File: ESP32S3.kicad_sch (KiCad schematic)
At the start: 0 parts

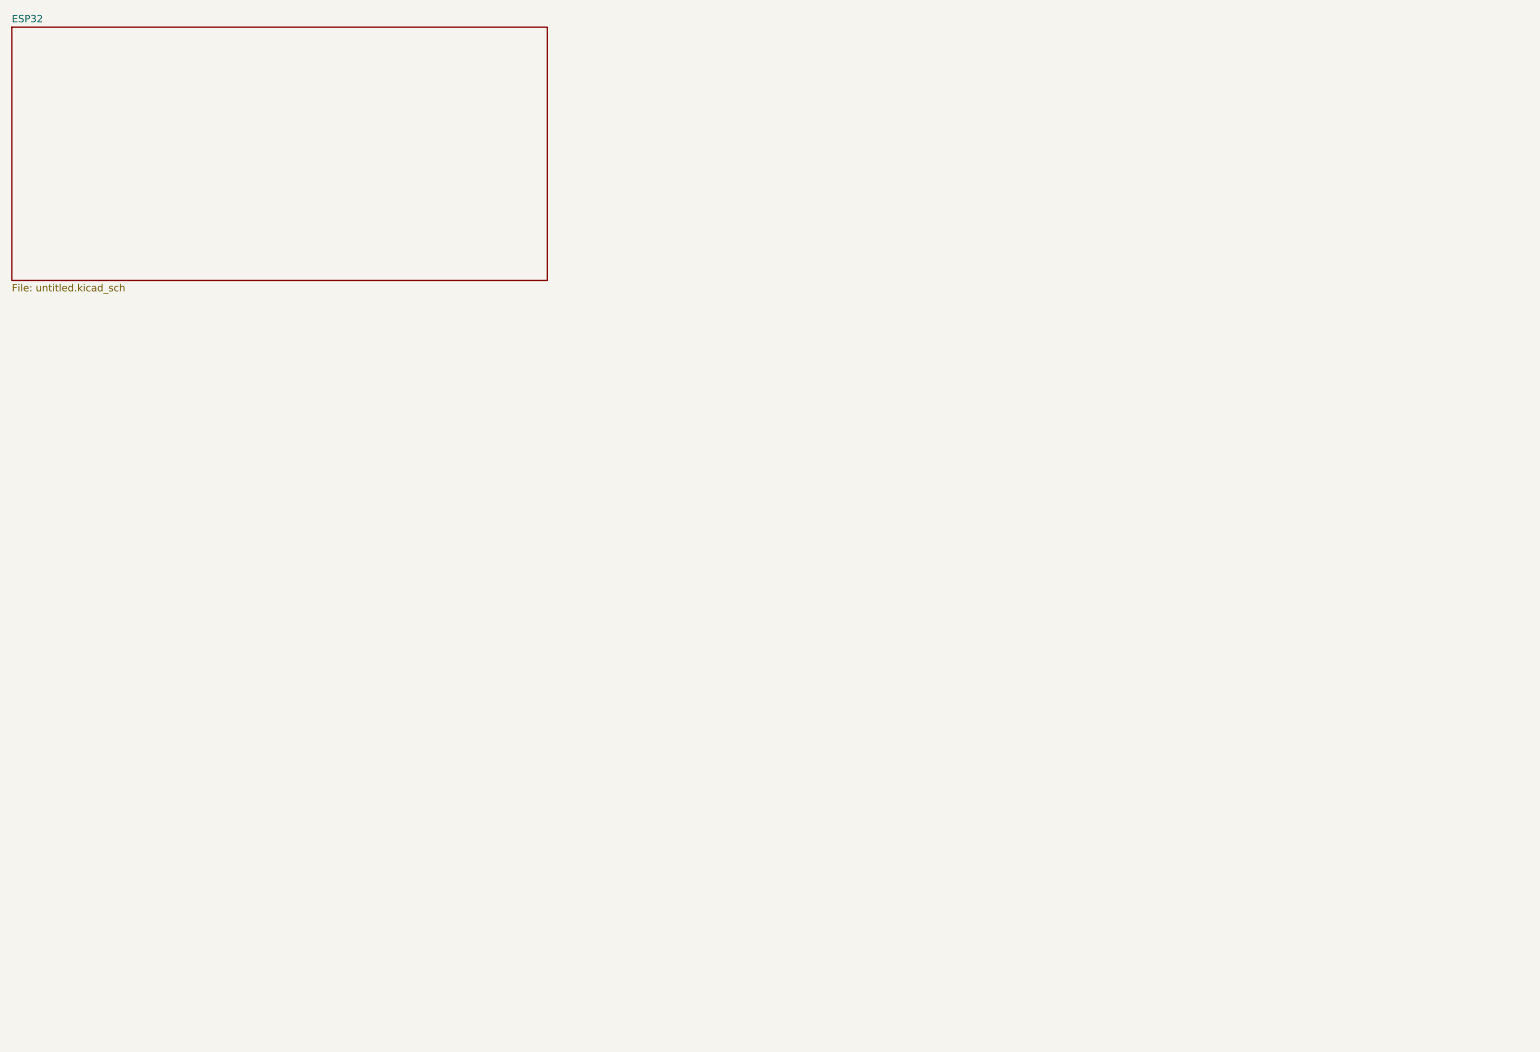
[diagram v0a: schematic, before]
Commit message: ESP32 module done
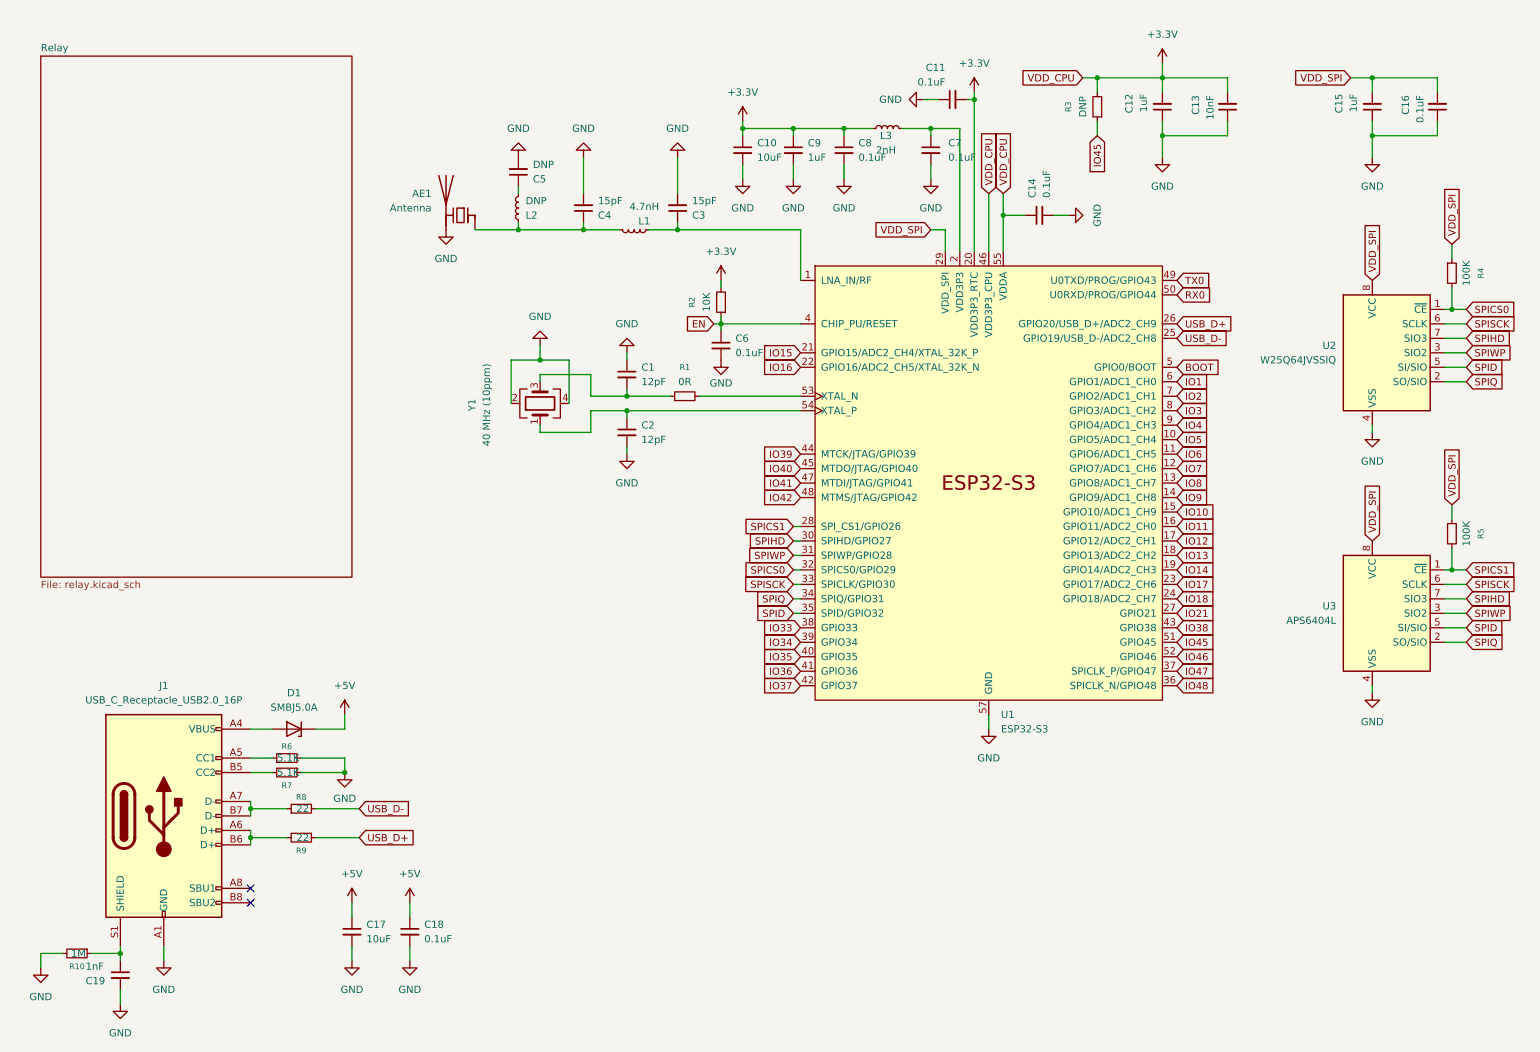
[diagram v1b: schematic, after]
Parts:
- added AE1: Antenna, RF_Antenna:Texas_SWRA117D_2.4GHz_Left, symbol Device:Antenna_Chip
- added C1, C2: 12pF, Capacitor_SMD:C_0603_1608Metric, symbol Device:C_Small
- added C10, C17: 10uF, Capacitor_SMD:C_0603_1608Metric, symbol Device:C_Small
- added C11, C14, C16, C18, C6, C7, C8: 0.1uF, Capacitor_SMD:C_0603_1608Metric, symbol Device:C_Small
- added C12, C15, C9: 1uF, Capacitor_SMD:C_0603_1608Metric, symbol Device:C_Small
- added C13: 10nF, Capacitor_SMD:C_0603_1608Metric, symbol Device:C_Small
- added C19: 1nF, Capacitor_SMD:C_0603_1608Metric, symbol Device:C_Small
- added C3, C4: 15pF, Capacitor_SMD:C_0603_1608Metric, symbol Device:C_Small
- added C5: DNP, Capacitor_SMD:C_0603_1608Metric, symbol Device:C_Small
- added D1: SMBJ5.0A, Diode_SMD:D_SMB, symbol Device:D_Zener
- added J1: USB_C_Receptacle_USB2.0_16P, Connector_USB:USB_C_Receptacle_G-Switch_GT-USB-7010ASV, symbol Connector:USB_C_Receptacle_USB2.0_16P
- added L1: 4.7nH, Inductor_SMD:L_0805_2012Metric, symbol Device:L_Small
- added L2: DNP, Inductor_SMD:L_0805_2012Metric, symbol Device:L_Small
- added L3: 2nH, Inductor_SMD:L_0805_2012Metric, symbol Device:L_Small
- added R1: 0R, Resistor_SMD:R_0603_1608Metric, symbol Device:R_Small
- added R10: 1M, Resistor_SMD:R_0603_1608Metric, symbol Device:R_Small
- added R2: 10K, Resistor_SMD:R_0603_1608Metric, symbol Device:R_Small
- added R3: DNP, Resistor_SMD:R_0603_1608Metric, symbol Device:R_Small
- added R4, R5: 100K, Resistor_SMD:R_0603_1608Metric, symbol Device:R_Small
- added R6, R7: 5.1K, Resistor_SMD:R_0603_1608Metric, symbol Device:R_Small
- added R8, R9: 22, Resistor_SMD:R_0603_1608Metric, symbol Device:R_Small
- added U1: ESP32-S3, Package_DFN_QFN:QFN-56-1EP_7x7mm_P0.4mm_EP5.6x5.6mm, symbol PCM_Espressif:ESP32-S3
- added U2: W25Q64JVSSIQ, Package_SO:SOP-8_3.9x4.9mm_P1.27mm, symbol Memory_RAM:ESP-PSRAM32
- added U3: APS6404L, Package_SO:SOP-8_3.9x4.9mm_P1.27mm, symbol Memory_RAM:ESP-PSRAM32
- added Y1: 40 MHz (10ppm), Crystal:Crystal_SMD_3225-4Pin_3.2x2.5mm, symbol Device:Crystal_GND24
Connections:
- new net: J1.A5 (CC1), R6.1
- new net: C2.1, U1.54 (XTAL_P), Y1.1
- new net: AE1.1 (FEED), C4.1, L1.1, L2.2
- new net: C3.1, L1.2, U1.1 (LNA_IN/RF)
- new net: C19.1, J1.S1 (SHIELD), R10.1
- new net: C5.1, L2.1
- new net: J1.A7 (D-), J1.B7 (D-), R8.1
- new net: D1.2 (A), J1.A4 (VBUS), J1.A9 (VBUS), J1.B4 (VBUS), J1.B9 (VBUS)
- new net: J1.A6 (D+), J1.B6 (D+), R9.2
- new net: J1.B5 (CC2), R7.2
- new net: C1.2, R1.1, Y1.3
- new net: R1.2, U1.53 (XTAL_N)
- new net +3.3V: C10.1, C11.2, C12.2, C13.2, C14.1, C8.1, C9.1, L3.2, R2.2, R3.2, U1.20 (VDD3P3_RTC), U1.46 (VDD3P3_CPU), U1.55 (VDDA), U1.56 (VDDA)
- new net +5V: C17.1, C18.1, D1.1 (K)
- new net BOOT: U1.5 (GPIO0/BOOT)
- new net EN: C6.1, R2.1, U1.4 (CHIP_PU/RESET)
- new net GND: AE1.2 (PCB_Trace), C1.1, C10.2, C11.1, C12.1, C13.1, C14.2, C15.1, C16.1, C17.2, C18.2, C19.2, C2.2, C3.2, C4.2, C5.2, C6.2, C7.2, C8.2, C9.2, J1.A1 (GND), J1.A12 (GND), J1.B1 (GND), J1.B12 (GND), R10.2, R6.2, R7.1, U1.57 (GND), U2.4 (VSS), U3.4 (VSS), Y1.2, Y1.4
- new net IO1: U1.6 (GPIO1/ADC1_CH0)
- new net IO10: U1.15 (GPIO10/ADC1_CH9)
- new net IO11: U1.16 (GPIO11/ADC2_CH0)
- new net IO12: U1.17 (GPIO12/ADC2_CH1)
- new net IO13: U1.18 (GPIO13/ADC2_CH2)
- new net IO14: U1.19 (GPIO14/ADC2_CH3)
- new net IO15: U1.21 (GPIO15/ADC2_CH4/XTAL_32K_P)
- new net IO16: U1.22 (GPIO16/ADC2_CH5/XTAL_32K_N)
- new net IO17: U1.23 (GPIO17/ADC2_CH6)
- new net IO18: U1.24 (GPIO18/ADC2_CH7)
- new net IO2: U1.7 (GPIO2/ADC1_CH1)
- new net IO21: U1.27 (GPIO21)
- new net IO3: U1.8 (GPIO3/ADC1_CH2)
- new net IO33: U1.38 (GPIO33)
- new net IO34: U1.39 (GPIO34)
- new net IO35: U1.40 (GPIO35)
- new net IO36: U1.41 (GPIO36)
- new net IO37: U1.42 (GPIO37)
- new net IO38: U1.43 (GPIO38)
- new net IO39: U1.44 (MTCK/JTAG/GPIO39)
- new net IO4: U1.9 (GPIO4/ADC1_CH3)
- new net IO40: U1.45 (MTDO/JTAG/GPIO40)
- new net IO41: U1.47 (MTDI/JTAG/GPIO41)
- new net IO42: U1.48 (MTMS/JTAG/GPIO42)
- new net IO45: R3.1, U1.51 (GPIO45)
- new net IO46: U1.52 (GPIO46)
- new net IO47: U1.37 (SPICLK_P/GPIO47)
- new net IO48: U1.36 (SPICLK_N/GPIO48)
- new net IO5: U1.10 (GPIO5/ADC1_CH4)
- new net IO6: U1.11 (GPIO6/ADC1_CH5)
- new net IO7: U1.12 (GPIO7/ADC1_CH6)
- new net IO8: U1.13 (GPIO8/ADC1_CH7)
- new net IO9: U1.14 (GPIO9/ADC1_CH8)
- new net RX0: U1.50 (U0RXD/PROG/GPIO44)
- new net SPICS0: R4.2, U1.32 (SPICS0/GPIO29), U2.1 (~{CE})
- new net SPICS1: R5.2, U1.28 (SPI_CS1/GPIO26), U3.1 (~{CE})
- new net SPID: U1.35 (SPID/GPIO32), U2.5 (SI/SIO), U3.5 (SI/SIO)
- new net SPIHD: U1.30 (SPIHD/GPIO27), U2.7 (SIO3), U3.7 (SIO3)
- new net SPIQ: U1.34 (SPIQ/GPIO31), U2.2 (SO/SIO), U3.2 (SO/SIO)
- new net SPISCK: U1.33 (SPICLK/GPIO30), U2.6 (SCLK), U3.6 (SCLK)
- new net SPIWP: U1.31 (SPIWP/GPIO28), U2.3 (SIO2), U3.3 (SIO2)
- new net TX0: U1.49 (U0TXD/PROG/GPIO43)
- new net USB_D+: R9.1, U1.26 (GPIO20/USB_D+/ADC2_CH9)
- new net USB_D-: R8.2, U1.25 (GPIO19/USB_D-/ADC2_CH8)
- new net VDD3P3: C7.1, L3.1, U1.2 (VDD3P3), U1.3 (VDD3P3)
- new net VDD_SPI: C15.2, C16.2, R4.1, R5.1, U1.29 (VDD_SPI), U2.8 (VCC), U3.8 (VCC)
- no-connect marks 0 -> 2
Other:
- removed sheet ESP32
- added sheet Relay (relay.kicad_sch)
